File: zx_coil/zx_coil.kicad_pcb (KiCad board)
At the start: 2 copper layers, 13.3 x 13.3 mm, 2 parts, among them T1 Coil

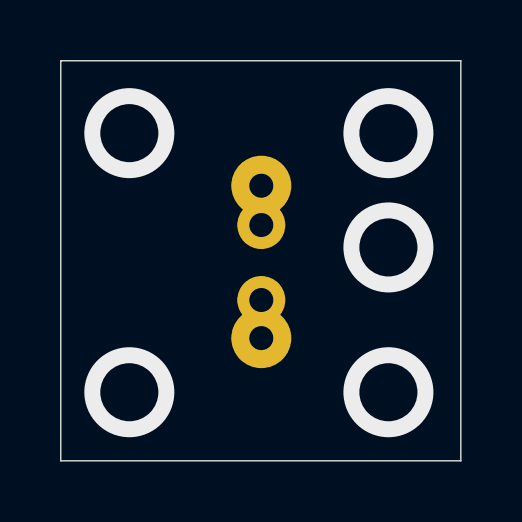
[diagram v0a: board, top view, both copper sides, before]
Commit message: reduced drill in coil
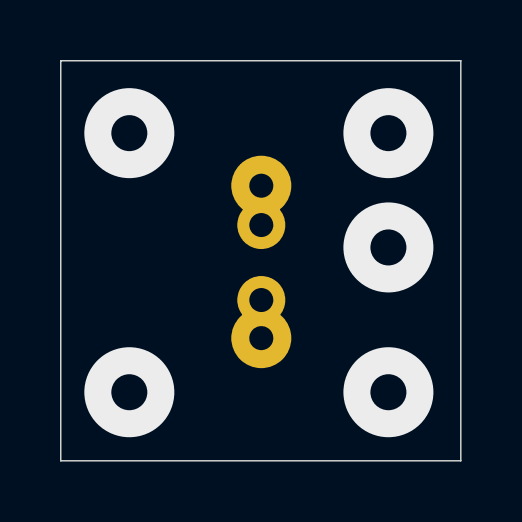
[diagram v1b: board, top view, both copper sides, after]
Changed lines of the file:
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@@
 		(at 129.032 75.311)
 		(size 3)
-		(drill 1.93548)
+		(drill 1.2)
 		(layers "F.Cu" "B.Cu")
 		(net 0)
@@
 		(at 129.032 83.947)
 		(size 3)
-		(drill 1.93548)
+		(drill 1.2)
 		(layers "F.Cu" "B.Cu")
 		(net 0)
@@
 		(at 137.668 83.947)
 		(size 3)
-		(drill 1.93548)
+		(drill 1.2)
 		(layers "F.Cu" "B.Cu")
 		(net 0)
@@
 		(at 137.668 79.121)
 		(size 3)
-		(drill 1.93548)
+		(drill 1.2)
 		(layers "F.Cu" "B.Cu")
 		(net 0)
@@
 		(at 137.668 75.311)
 		(size 3)
-		(drill 1.93548)
+		(drill 1.2)
 		(layers "F.Cu" "B.Cu")
 		(net 0)
